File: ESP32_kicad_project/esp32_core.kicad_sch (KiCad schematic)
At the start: 1 part, among them U2 ESP32-WROOM-32E

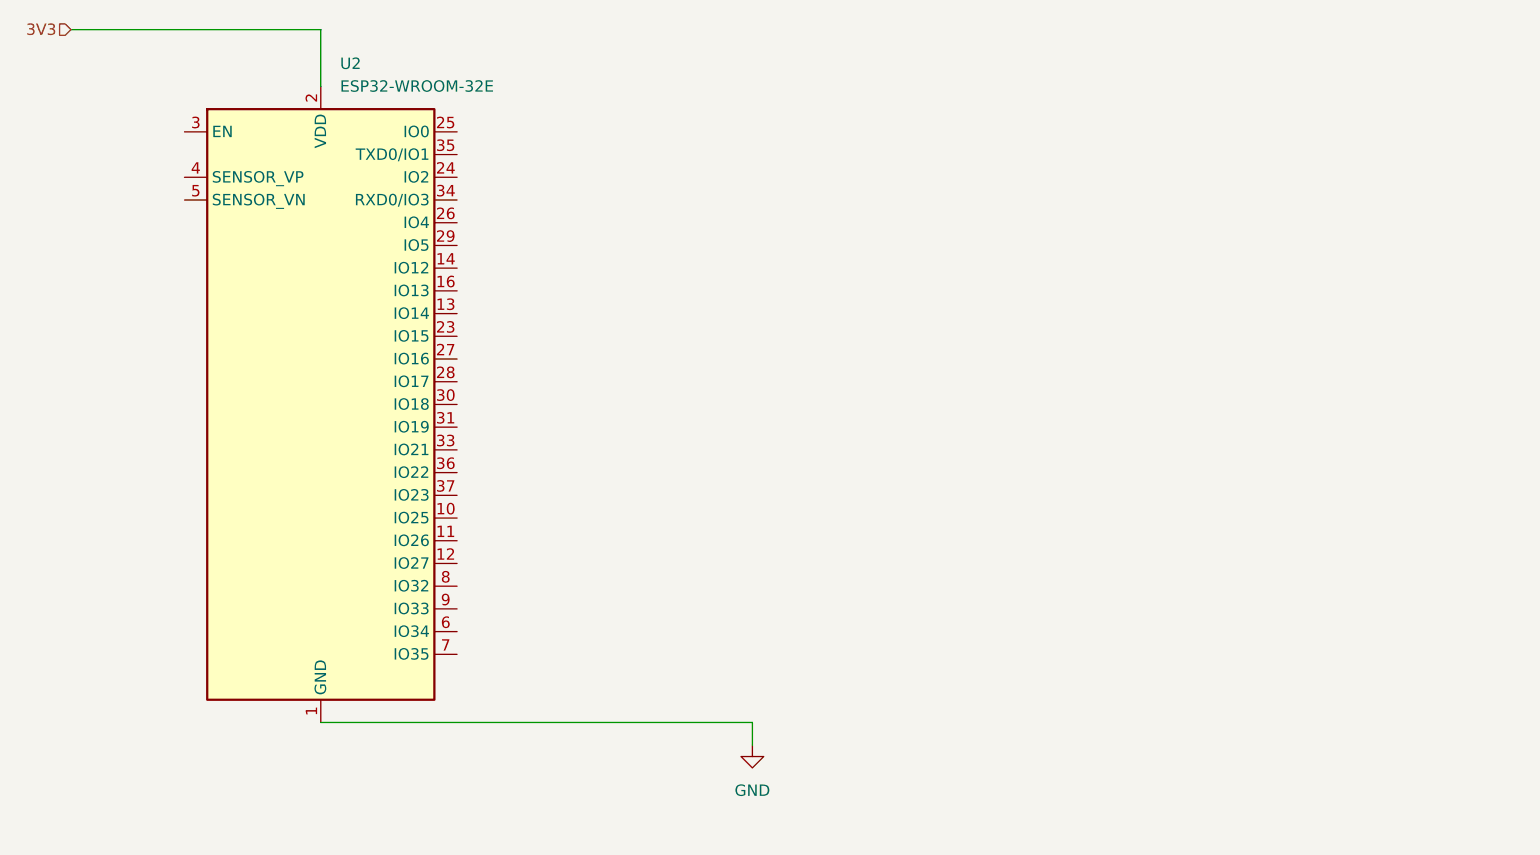
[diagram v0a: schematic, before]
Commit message: optimized everything with hierarchical labels, completed esp core, assigned footprints everywhere
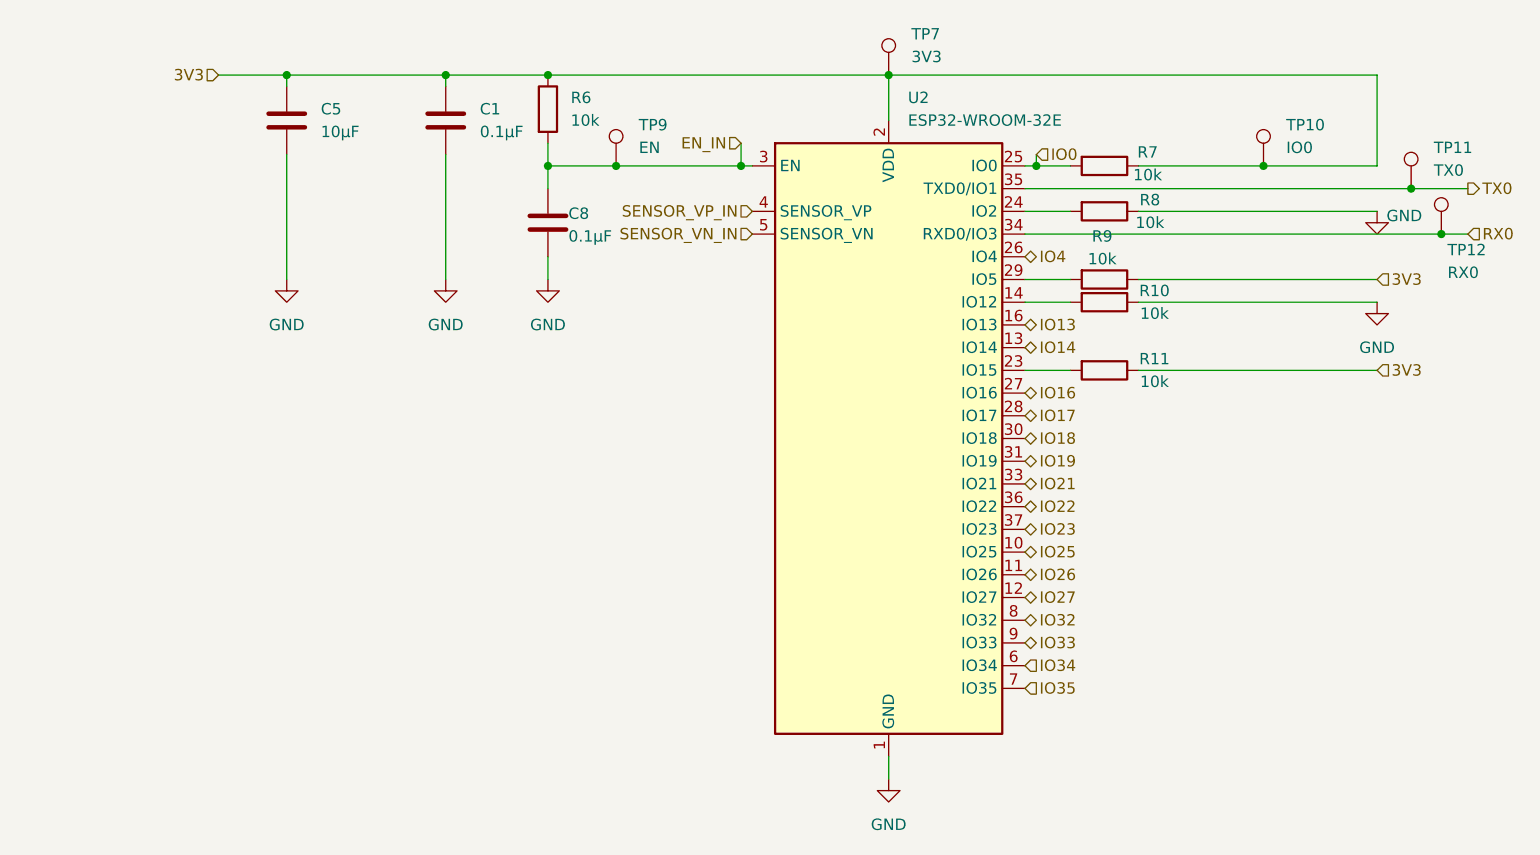
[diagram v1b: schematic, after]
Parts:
- added C1, C8: 0.1µF, Capacitor_SMD:C_0603_1608Metric, symbol Device:C
- added C5: 10µF, Capacitor_SMD:C_0805_2012Metric, symbol Device:C
- added R10, R11, R6, R7, R8, R9: 10k, Resistor_SMD:R_0603_1608Metric, symbol Device:R
- added TP10: IO0, TestPoint:TestPoint_Pad_D1.5mm, symbol Connector:TestPoint
- added TP11: TX0, TestPoint:TestPoint_Pad_D1.5mm, symbol Connector:TestPoint
- added TP12: RX0, TestPoint:TestPoint_Pad_D1.5mm, symbol Connector:TestPoint
- added TP7: 3V3, TestPoint:TestPoint_Pad_D1.5mm, symbol Connector:TestPoint
- added TP9: EN, TestPoint:TestPoint_Pad_D1.5mm, symbol Connector:TestPoint
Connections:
- net 3V3: now also C1.1, C5.1, R11.1, R6.1, R7.1, R9.1, TP10.1, TP7.1
- net GND: now also C1.2, C5.2, C8.2, R10.1, R8.1
- net IO25: now reaches U2.10 (IO25)
- net IO26: now reaches U2.11 (IO26)
- net IO27: now reaches U2.12 (IO27)
- net IO14: now reaches U2.13 (IO14)
- net at U2.14 (IO12): now also R10.2
- net IO13: now reaches U2.16 (IO13)
- net at U2.23 (IO15): now also R11.2
- net at U2.24 (IO2): now also R8.2
- net IO0: now reaches U2.25 (IO0)
- net IO0: now also R7.2
- net IO4: now reaches U2.26 (IO4)
- net IO16: now reaches U2.27 (IO16)
- net IO17: now reaches U2.28 (IO17)
- net at U2.29 (IO5): now also R9.2
- net EN_IN: now reaches U2.3 (EN)
- net EN_IN: now also C8.1, R6.2, TP9.1
- net IO18: now reaches U2.30 (IO18)
- net IO19: now reaches U2.31 (IO19)
- net IO21: now reaches U2.33 (IO21)
- net RX0: now reaches U2.34 (RXD0/IO3)
- net RX0: now also TP12.1
- net TX0: now reaches U2.35 (TXD0/IO1)
- net TX0: now also TP11.1
- net IO22: now reaches U2.36 (IO22)
- net IO23: now reaches U2.37 (IO23)
- net SENSOR_VP_IN: now reaches U2.4 (SENSOR_VP)
- net SENSOR_VN_IN: now reaches U2.5 (SENSOR_VN)
- net IO34: now reaches U2.6 (IO34)
- net IO35: now reaches U2.7 (IO35)
- net IO32: now reaches U2.8 (IO32)
- net IO33: now reaches U2.9 (IO33)
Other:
- moved on the sheet: U2
